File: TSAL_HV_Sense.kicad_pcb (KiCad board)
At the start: 2 copper layers, 50 x 100 mm, 24 parts, among them J1 2-1445098-2, J2 Conn_01x03, J3 2-1445098-2, J4 Conn_01x03, J5 Conn_01x06, U1 4N35, U2 4N35

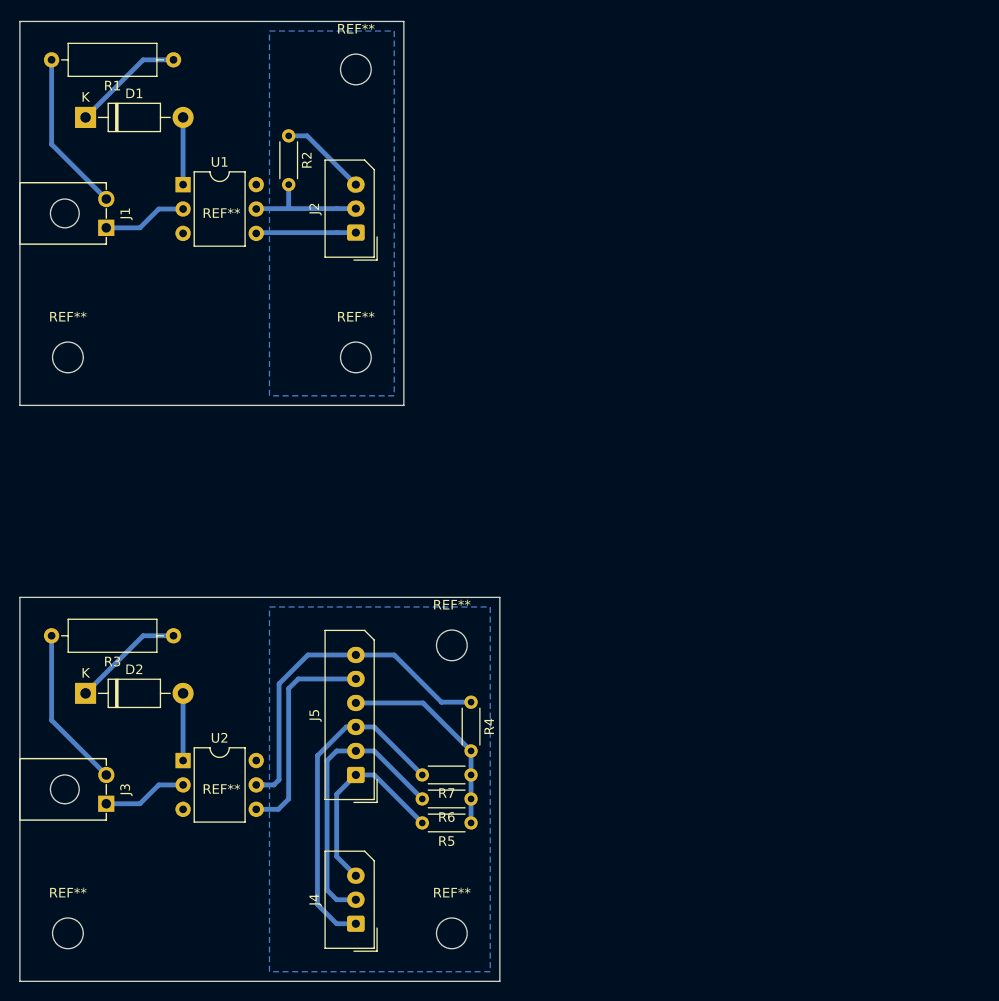
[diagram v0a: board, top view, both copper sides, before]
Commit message: Redo HV sense boards
- added circuitry & connector for ts active led
- added led indicators for relay aux
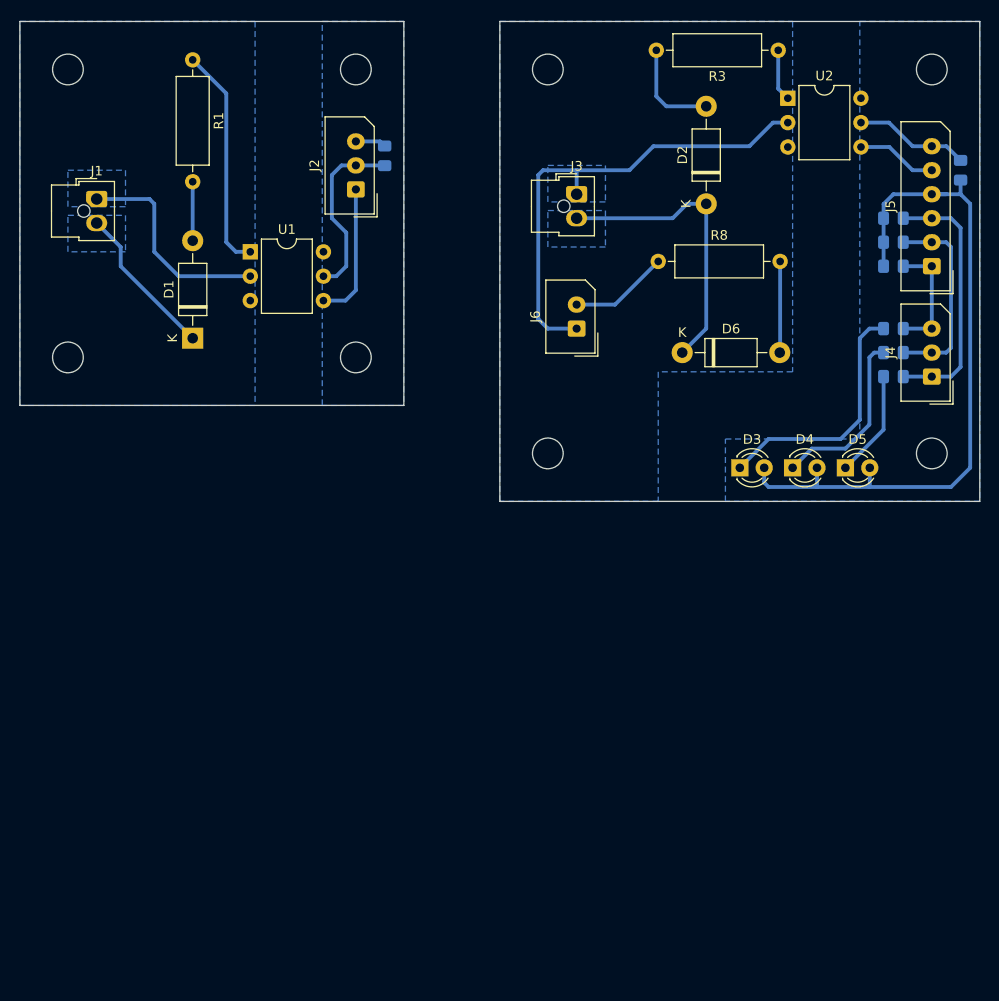
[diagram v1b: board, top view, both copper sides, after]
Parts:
- removed the REF** at (85.0, 135.0)
- removed the REF** at (61.0, 119.5)
- removed the REF** at (45.0, 135.0)
- removed the REF** at (61.0, 59.5)
- added  : MountingHole_3.2mm_M3, MountingHole:MountingHole_3.2mm_M3, F.Cu at (45.0, 45.0)
- added D3: LED, LED_THT:LED_D3.0mm, F.Cu at (115.0, 86.5)
- added D4: LED, LED_THT:LED_D3.0mm, F.Cu at (120.5, 86.5)
- added D5: LED, LED_THT:LED_D3.0mm, F.Cu at (126.0, 86.5)
- added D6: 51V, Diode_THT:D_DO-41_SOD81_P10.16mm_Horizontal, F.Cu at (109.0, 74.5)
- added J6: Conn_01x02, Connector_Molex:Molex_SPOX_5267-02A_1x02_P2.50mm_Vertical, F.Cu at (98.0, 72.0)
- added R10: 10k, Resistor_SMD:R_0805_2012Metric_Pad1.15x1.40mm_HandSolder, B.Cu at (131.0, 74.5)
- added R11: 10k, Resistor_SMD:R_0805_2012Metric_Pad1.15x1.40mm_HandSolder, B.Cu at (131.0, 77.0)
- added R8: 4.7k, Resistor_THT:R_Axial_DIN0309_L9.0mm_D3.2mm_P12.70mm_Horizontal, F.Cu at (106.5, 65.0)
- added R9: 10k, Resistor_SMD:R_0805_2012Metric_Pad1.15x1.40mm_HandSolder, B.Cu at (131.0, 72.0)
- added REF**: Cutout, project:Cutout, F.Cu at (124.0, 50.5)
- added REF**: Cutout, project:Cutout, F.Cu at (68.0, 66.5)
- added REF**: MountingHole_3.2mm_M3, MountingHole:MountingHole_3.2mm_M3, F.Cu at (95.0, 45.0)
- added REF**: MountingHole_3.2mm_M3, MountingHole:MountingHole_3.2mm_M3, F.Cu at (135.0, 85.0)
- added REF**: MountingHole_3.2mm_M3, MountingHole:MountingHole_3.2mm_M3, F.Cu at (95.0, 85.0)
-  : renamed from REF**
- J1, J3: value 2-1445098-2 -> Nano-Fit; footprint project:TE_2-1445098-2 -> Connector_Molex:Molex_Nano-Fit_105309-xx02_1x02_P2.50mm_Vertical
- J2, J4: value Conn_01x03 -> 22035035
- J5: value Conn_01x06 -> 22035065
- R2, R4, R5, R6, R7: footprint Resistor_THT:R_Axial_DIN0204_L3.6mm_D1.6mm_P5.08mm_Horizontal -> Resistor_SMD:R_0805_2012Metric_Pad1.15x1.40mm_HandSolder; moved to B.Cu
- moved U2 93.4 mm to (120.0, 48.0)
- moved R3 87.7 mm to (119.0, 43.0)
- moved J4 82.8 mm to (135.0, 77.0)
- moved D2 82.4 mm to (111.5, 59.0), turned to 90 degrees
- moved J5 80.1 mm to (135.0, 65.5)
- moved J3 79.0 mm to (98.0, 58.0), turned to 0 degrees
- moved REF** 78.1 mm to (135.0, 45.0)
- moved R4 75.3 mm to (138.0, 55.5)
- moved R5 72.8 mm to (131.0, 65.5), turned to 0 degrees
- moved R6 72.8 mm to (131.0, 63.0), turned to 0 degrees
- moved R7 72.8 mm to (131.0, 60.5), turned to 0 degrees
- moved D1 25.6 mm to (58.0, 73.0), turned to 90 degrees
- moved R2 10.2 mm to (78.0, 54.0)
- moved U1 9.90 mm to (64.0, 64.0)
- moved J2 4.50 mm to (75.0, 57.5)
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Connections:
- D1 pad 1: Net-(D1-Pad1) -> /HV+
- D2 pad 1: Net-(D2-Pad1) -> /HV+
- R1 pad 1: Net-(D1-Pad1) -> Net-(R1-Pad1)
- R1 pad 2: /HV+ -> Net-(D1-Pad2)
- R3 pad 1: Net-(D2-Pad1) -> Net-(R3-Pad1)
- R3 pad 2: /HV+ -> Net-(D2-Pad2)
- U1 pad 1: Net-(D1-Pad2) -> Net-(R1-Pad1)
- U2 pad 1: Net-(D2-Pad2) -> Net-(R3-Pad1)
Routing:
- net /HV-: track 17.6 -> 72.4 mm
- net /VCC: track 30.7 -> 78.1 mm
- net Net-(D3-Pad1): track 0.00 -> 26.0 mm
- net Net-(R1-Pad1): track 0.00 -> 23.4 mm
- net /Sense: track 49.6 -> 30.9 mm
- net Net-(D4-Pad1): track 0.00 -> 18.5 mm
- net /HV+: track 33.7 -> 46.8 mm
- net Net-(D2-Pad1): track 11.6 -> 0.00 mm
- net Net-(D1-Pad1): track 11.6 -> 0.00 mm
- net Net-(D5-Pad1): track 0.00 -> 11.1 mm
- net /GND: track 33.2 -> 22.7 mm
- net Net-(J6-Pad2): track 0.00 -> 10.4 mm
- net Net-(D6-Pad2): track 0.00 -> 9.52 mm
- net /AUX_3: track 21.1 -> 12.4 mm
- net /AUX_2: track 29.3 -> 20.9 mm
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- added copper zone on B.Cu, net /HV+
- added copper zone on B.Cu, net /HV-
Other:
- board size 50 x 100 mm -> 100 x 50 mm
- net class Default: trace_width 0.5 -> 0.4; via_dia 0.8 -> 1.4; via_drill 0.4 -> 0.7
- net class HV added: clearance 0.6, trace_width 0.4, via_dia 1.4, via_drill 0.7

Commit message: tsal sense board update
hopefully last update
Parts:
- removed the D3 at (115.0, 86.5)
- removed the R8 at (106.5, 65.0)
- removed the R9 at (131.0, 72.0)
- removed the REF** at (124.0, 50.5)
- removed the REF** at (68.0, 66.5)
- added D4: LED, LED_THT:LED_D3.0mm, F.Cu at (115.0, 86.5)
- added R11: 1k, Resistor_SMD:R_0805_2012Metric_Pad1.15x1.40mm_HandSolder, B.Cu at (131.0, 74.5)
- added R4: 2k, Resistor_THT:R_Axial_DIN0309_L9.0mm_D3.2mm_P12.70mm_Horizontal, F.Cu at (106.0, 68.0)
- added R5: 2k, Resistor_THT:R_Axial_DIN0309_L9.0mm_D3.2mm_P12.70mm_Horizontal, F.Cu at (106.0, 74.0)
- added REF**: Cutout, project:Cutout, F.Cu at (123.8, 50.5)
- added REF**: Cutout, project:Cutout, F.Cu at (67.8, 66.5)
- D3: renamed from D6; value 51V -> 30V
- J2: value 22035035 -> Mini-SPOX
- J4: renamed from J6; value Conn_01x02 -> Mini-SPOX
- J5: renamed from J4; value 22035035 -> Mini-SPOX
- J6: renamed from J5; value 22035065 -> Mini-SPOX
- R10: value 10k -> 1k
- R12: renamed from R11; value 10k -> 1k
- moved D3 12.9 mm to (106.0, 62.0)
- moved R10 2.50 mm to (131.0, 72.0)
- moved D2 1.91 mm to (112.0, 57.2)
- moved R2 0.25 mm to (78.0, 53.8)
- renumbered D4 to D5, D5 to D6, R4 to R6, R5 to R7, R6 to R8, R7 to R9
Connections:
- D5 pad 1: Net-(D4-Pad1) -> Net-(D5-Pad1)
- R10 pad 1: /AUX_2 -> /AUX_3
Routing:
- net Net-(D3-Pad1): track 26.0 -> 0.00 mm
- net Net-(D5-Pad1): track 0.00 -> 18.5 mm
- net Net-(R4-Pad1): track 0.00 -> 15.2 mm
- net /HV+: track 46.8 -> 35.6 mm
- net Net-(D4-Pad1): track 18.5 -> 26.0 mm
- net /HV-: track 72.4 -> 67.0 mm
- net Net-(D2-Pad2): track 10.4 -> 7.36 mm
- net Net-(D3-Pad2): track 9.52 -> 7.05 mm
- net Net-(R1-Pad1): track 23.4 -> 22.5 mm
- net Net-(J4-Pad2): track 10.4 -> 9.86 mm
- removed copper zone on B.Cu, net (none)
- removed copper zone on B.Cu, net /HV+
- removed copper zone on B.Cu, net /HV-
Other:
- board text added: "+"
- board text added: "-"
- board text added: "AIR Aux"
- board text added: "HV IN"
- board text added: "LED OUT"
- board text added: "LV"
- board text added: "OUR TSAL HV Sense Battery"
- board text added: "OUR TSAL HV Sense HVJB"
- board text added: "TS"
- board text added: "To TSAL Logic"

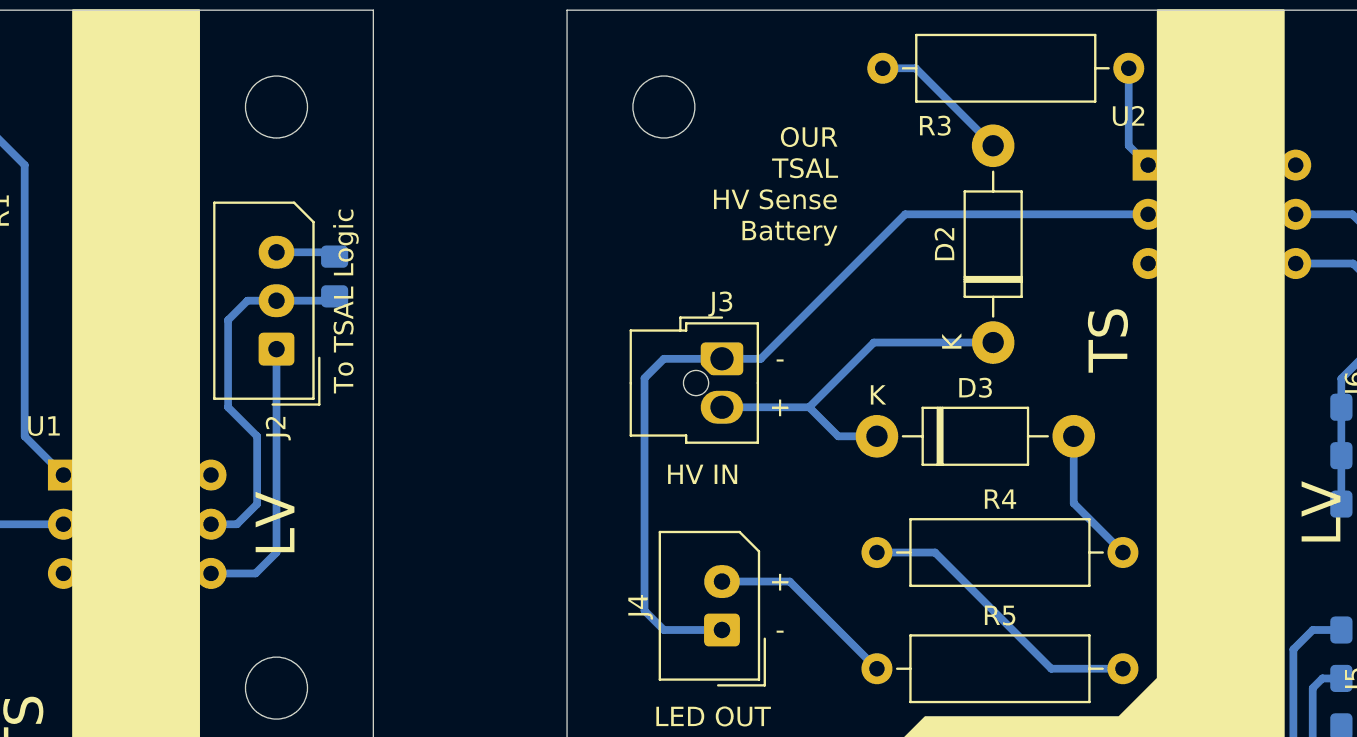
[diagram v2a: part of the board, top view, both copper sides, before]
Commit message: use outline layer for cutout
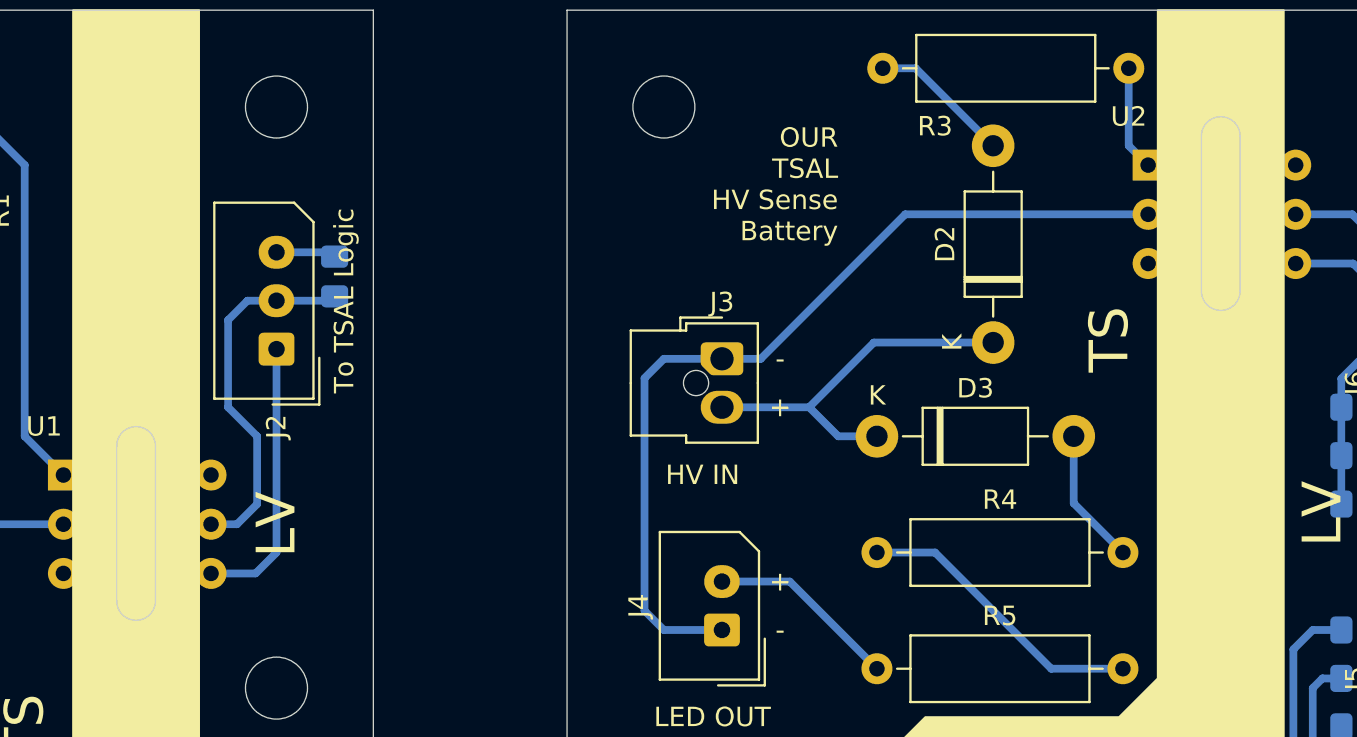
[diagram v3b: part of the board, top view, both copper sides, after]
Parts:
- removed the REF** at (123.8, 50.5)
- removed the REF** at (67.8, 66.5)
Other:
- outline, holes or cut-outs redrawn
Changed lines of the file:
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@@
   (general
     (thickness 1.6)
-    (drawings 30)
+    (drawings 38)
     (tracks 111)
     (zones 0)
-    (modules 36)
+    (modules 34)
     (nets 19)
   )
@@
     (34 B.Paste user hide)
     (35 F.Paste user hide)
-    (36 B.SilkS user)
-    (37 F.SilkS user)
+    (36 B.SilkS user hide)
+    (37 F.SilkS user hide)
     (38 B.Mask user)
     (39 F.Mask user)
@@
     (add_net "Net-(J4-Pad2)")
     (add_net "Net-(R4-Pad1)")
-    (add_net "Net-(U1-Pad3)")
-    (add_net "Net-(U1-Pad6)")
-    (add_net "Net-(U2-Pad3)")
-    (add_net "Net-(U2-Pad6)")
   )
   (net_class HV ""
@@
     (add_net "Net-(R1-Pad1)")
     (add_net "Net-(R3-Pad1)")
-  )
-  (module project:Cutout (layer F.Cu)
-    (at 123.75 50.5)
-    (fp_text reference REF** (at 0 0.5) (layer F.SilkS) hide
-      (effects (font (size 1 1) (thickness 0.15)))
-    )
-    (fp_text value Cutout (at 0 -0.5) (layer F.Fab)
-      (effects (font (size 1 1) (thickness 0.15)))
-    )
-    (pad "" np_thru_hole oval (at 0 0) (size 2 10) (drill oval 2 10) (layers *.Cu *.Mask))
-  )
-  (module project:Cutout locked (layer F.Cu)
-    (at 67.75 66.5)
-    (fp_text reference REF** (at 0 0.5) (layer F.SilkS) hide
-      (effects (font (size 1 1) (thickness 0.15)))
-    )
-    (fp_text value Cutout (at 0 -0.5) (layer F.Fab)
-      (effects (font (size 1 1) (thickness 0.15)))
-    )
-    (pad "" np_thru_hole oval (at 0 0) (size 2 10) (drill oval 2 10) (layers *.Cu *.Mask))
   )
   (module MountingHole:MountingHole_3.2mm_M3 locked (layer F.Cu)
@@
     )
   )
+  (gr_line (start 122.75 46.5) (end 122.75 54.5) (layer Edge.Cuts) (width 0.05))
+  (gr_line (start 124.75 54.5) (end 124.75 46.5) (layer Edge.Cuts) (width 0.05))
+  (gr_arc (start 123.75 54.5) (end 122.75 54.5) (angle -180) (layer Edge.Cuts) (width 0.05))
+  (gr_arc (start 123.75 46.5) (end 124.75 46.5) (angle -180) (layer Edge.Cuts) (width 0.05))
+  (gr_line (start 68.75 70.5) (end 68.75 62.5) (layer Edge.Cuts) (width 0.05))
+  (gr_line (start 66.75 62.5) (end 66.75 70.5) (layer Edge.Cuts) (width 0.05))
+  (gr_arc (start 67.75 70.5) (end 66.75 70.5) (angle -180) (layer Edge.Cuts) (width 0.05))
+  (gr_arc (start 67.75 62.5) (end 68.75 62.5) (angle -180) (layer Edge.Cuts) (width 0.05))
   (gr_text LV (at 75 66.55 90) (layer F.SilkS)
     (effects (font (size 2 2) (thickness 0.3)))
@@
   (segment (start 58 44) (end 62 48) (width 0.4) (layer B.Cu) (net 14))
   (segment (start 62 48) (end 62 62) (width 0.4) (layer B.Cu) (net 14))
+  (segment (start 116.16 65.46) (end 118.7 68) (width 0.4) (layer B.Cu) (net 15))
+  (segment (start 116.16 62) (end 116.16 65.46) (width 0.4) (layer B.Cu) (net 15))
   (segment (start 129.975 82.525) (end 126 86.5) (width 0.4) (layer B.Cu) (net 16))
   (segment (start 129.975 77) (end 129.975 82.525) (width 0.4) (layer B.Cu) (net 16))
-  (segment (start 116.16 65.46) (end 118.7 68) (width 0.4) (layer B.Cu) (net 15))
-  (segment (start 116.16 62) (end 116.16 65.46) (width 0.4) (layer B.Cu) (net 15))
   (segment (start 101.5 69.5) (end 106 74) (width 0.4) (layer B.Cu) (net 17))
   (segment (start 98 69.5) (end 101.5 69.5) (width 0.4) (layer B.Cu) (net 17))

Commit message: oops obsolete part
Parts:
- D3: value 30V -> 33V
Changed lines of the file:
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@@
     (add_net "Net-(J4-Pad2)")
     (add_net "Net-(R4-Pad1)")
+    (add_net "Net-(U1-Pad3)")
+    (add_net "Net-(U1-Pad6)")
+    (add_net "Net-(U2-Pad3)")
+    (add_net "Net-(U2-Pad6)")
   )
   (net_class HV ""
@@
       (effects (font (size 1 1) (thickness 0.15)))
     )
-    (fp_text value 30V (at 5.08 2.47) (layer F.Fab)
+    (fp_text value 33V (at 5.08 2.47) (layer F.Fab)
       (effects (font (size 1 1) (thickness 0.15)))
     )
